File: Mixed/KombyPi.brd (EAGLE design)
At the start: 63.2 x 57.1 mm, 16 parts, among them IC3 DS1307, J1 POWER_JACKPTH, J2 MOLEX-39501XXX4, Q1 32.768

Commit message: Update KombyPi mixed boards to be cleaner layout.
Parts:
- removed BAT: CR1220, adafruit:CR1220-THM
- removed C1: 0.1uF, adafruit:C025-025X050
- removed IC3: DS1307, adafruit:DIL08
- removed JP3: RASPBERRYPI-B+-GPIO, SparkFun-Boards:2X20-SHROUDED
- removed Q1: 32.768, crystal:TC38H
- added JP1: RASPBERRYPI-GPIOPTH, SparkFun-Boards:2X13-SHROUDED
- added U$2: (no value), holes:3,6
- added U$3: (no value), DIYChristmas-org:DIYC
- U$1: device DIYChristmas-org:DIYC -> holes:3,6
- moved C4 55.4 mm to (7.62, 38.1), turned to 270 degrees
- moved C2 52.4 mm to (54.6, 50.8)
- moved C3 40.9 mm to (47.0, 50.8)
- moved J2 39.6 mm to (30.5, 6.35), turned to 0 degrees
- moved V1 33.8 mm to (20.3, 38.1), turned to 0 degrees
- moved F2 24.4 mm to (30.5, 16.5), turned to 180 degrees
- moved JP4 19.1 mm to (50.8, 40.6)
- moved U$1 13.5 mm to (29.2, 25.4)
- moved FTDI 6.35 mm to (8.89, 17.8), turned to 0 degrees
- moved D1 1.80 mm to (17.8, 5.08)
- moved J1 1.27 mm to (7.62, -3.17)
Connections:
- removed net N$14: IC3.1, Q1.2
- removed net N$15: IC3.2, Q1.1
- removed net N$39: BAT.+2, IC3.3
- removed net SQW: IC3.7
- new net WS2801_VCC_FUSED: F2.P$1, F2.P$2, J2.4
- net 3.3V: now also JP1.1, JP1.17; no longer JP3.1, JP3.17
- net CE0: now also JP1.24; no longer JP3.24
- net CE1: now also JP1.26; no longer JP3.26
- net GND: now also JP1.14, JP1.20, JP1.25, JP1.6, JP1.9; no longer BAT.-, C1.2, IC3.4, JP3.14, JP3.20, JP3.25, JP3.30, JP3.34, JP3.39, JP3.6, JP3.9
- net MISO: now also JP1.21; no longer JP3.21
- net MOSI: now also JP1.19; no longer JP3.19
- net RF_CE: now also JP1.15; no longer JP3.15
- net RXI: now also JP1.10; no longer JP3.10
- net SCL: now also JP1.5; no longer IC3.6, JP3.5
- net SCLK: now also JP1.23; no longer JP3.23
- net SDA: now also JP1.3; no longer IC3.5, JP3.3
- net TXO: now also JP1.8; no longer JP3.8
- net VCC: now also JP1.2, JP1.4; no longer C1.1, D1.C, F2.P$3, F2.P$4, IC3.8, JP3.2, JP3.4
- net WS2801_VCC: now also D1.C, F2.P$3, F2.P$4; no longer F2.P$1, F2.P$2, J2.4
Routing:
- net N$39: track 33.0 -> 0.00 mm
- net CE1: track 58.4 -> 27.0 mm, vias 1 -> 0
- net MOSI: track 34.0 -> 59.1 mm
- net MISO: track 9.94 -> 34.6 mm
- net SDA: track 24.2 -> 0.00 mm
- net SCL: track 23.5 -> 0.00 mm
- net WS2801_SCLK: track 16.1 -> 35.1 mm
- net N$3: track 0.00 -> 17.7 mm
- net WS2801_MOSI: track 20.2 -> 37.5 mm
- net RF_CE: track 15.0 -> 31.9 mm, vias 0 -> 1
- net WS2801_VCC_FUSED: track 0.00 -> 13.8 mm
- net 3.3V: track 29.2 -> 42.1 mm, vias 0 -> 1
- net SCLK: track 50.5 -> 61.6 mm
- net TXO: track 43.8 -> 53.1 mm
- net N$14: track 8.45 -> 0.00 mm
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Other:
- board size 63.2 x 57.1 mm -> 59.4 x 57.1 mm
- board text added: "(c) 2015 Mat Mrosko"
- board text added: "B"
- board text added: "B+"

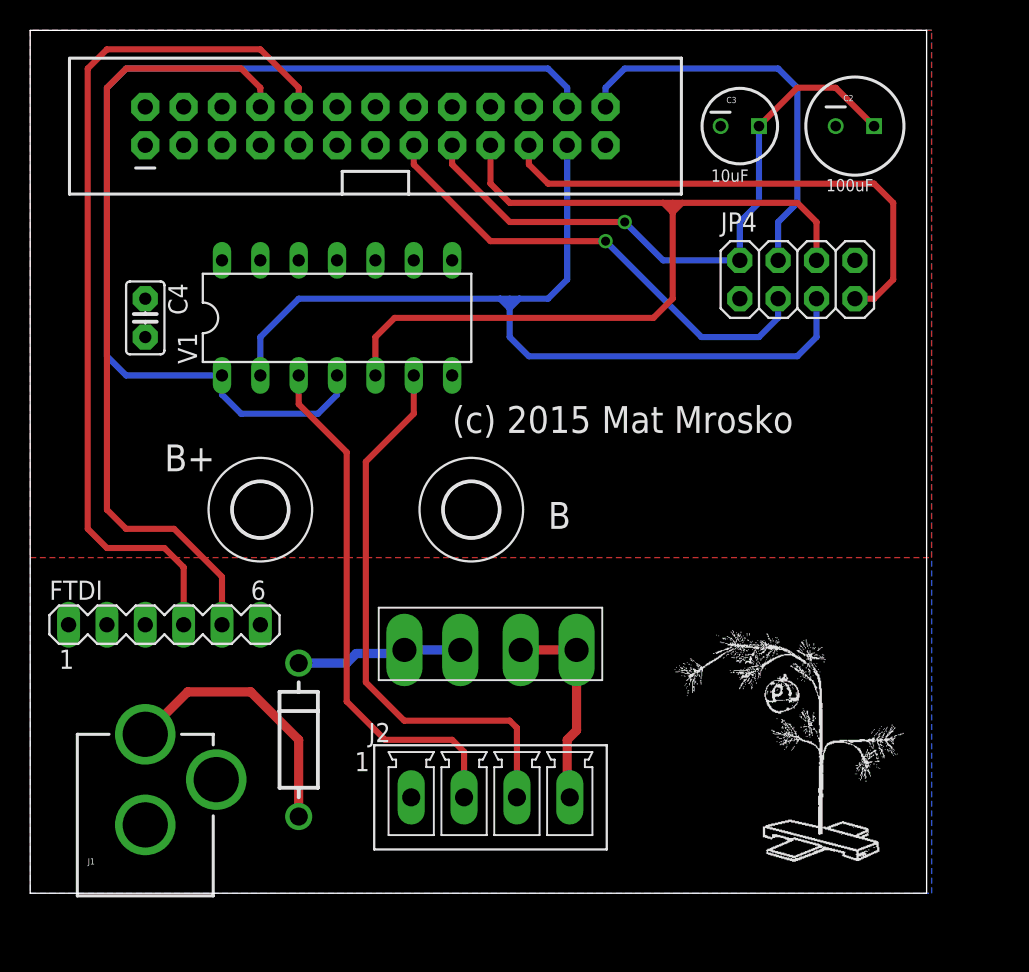
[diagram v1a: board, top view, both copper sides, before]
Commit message: Update KombyPi to have proper orientation for nRF
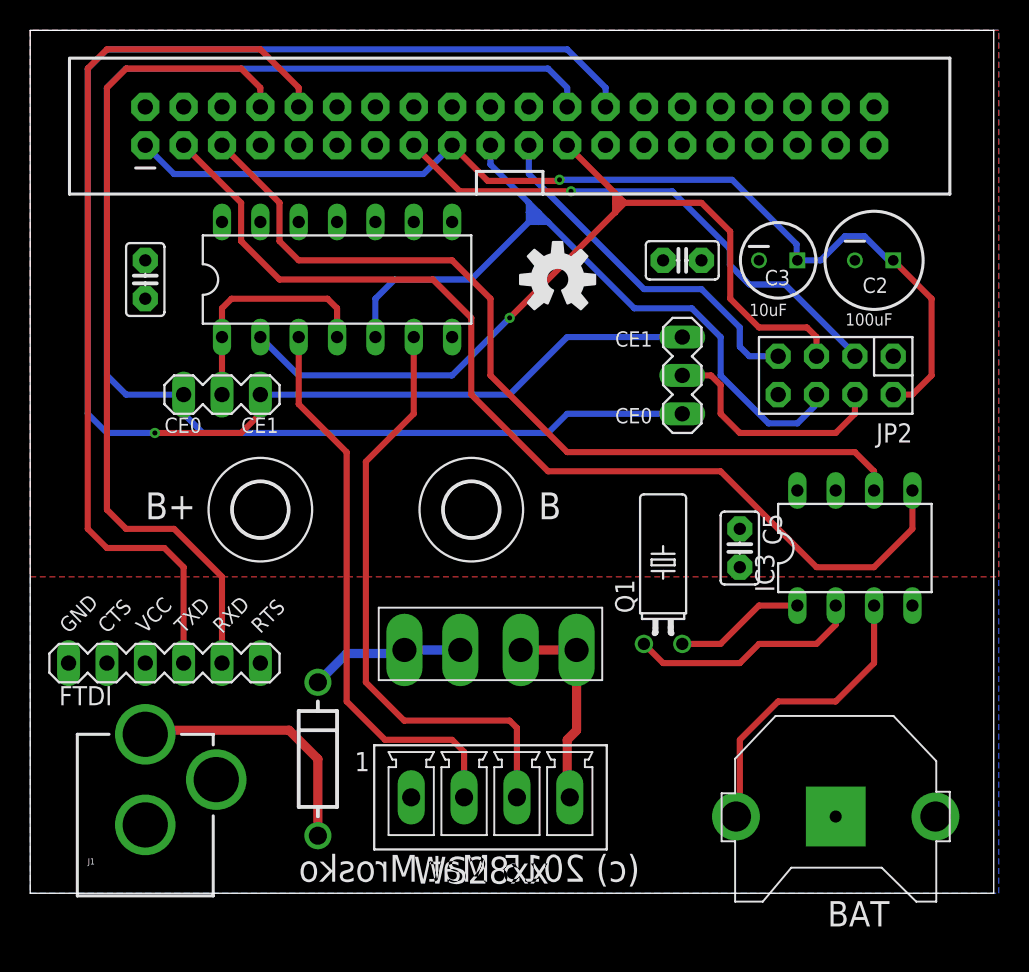
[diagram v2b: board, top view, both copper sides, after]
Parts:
- removed JP4: (no value), adafruit:2X04
- added BAT: CR1220, adafruit:CR1220-THM
- added C1, C5: 0.1uF, adafruit:C025-025X050
- added IC3: DS1307, adafruit:DIL08
- added JP2: (no value), Materdaddy-Custom:2X04
- added Q1: 32.768, crystal:TC38H
- added SV1, SV2: (no value), Materdaddy-Custom:MA03-1
- FTDI: device con-lstb:MA06-1 -> Materdaddy-Custom:MA06-1
- JP1: value RASPBERRYPI-GPIOPTH -> RASPBERRYPI-B+-GPIO; device SparkFun-Boards:2X13-SHROUDED -> SparkFun-Boards:2X20-SHROUDED
- U$3: device DIYChristmas-org:DIYC -> SparkFun-Aesthetics:OSHW-LOGO-M
- moved U$3 40.0 mm to (34.9, 40.6)
- moved C3 9.25 mm to (49.5, 41.9)
- moved C2 8.98 mm to (55.9, 41.9)
- moved JP1 8.89 mm to (31.8, 50.8)
- moved FTDI 2.54 mm to (8.89, 15.2)
- moved C4 2.54 mm to (7.62, 40.6)
- moved V1 2.54 mm to (20.3, 40.6)
- moved D1 1.80 mm to (19.1, 3.81)
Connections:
- new net +3V3: C1.1
- new net N$14: IC3.1, Q1.2
- new net N$15: IC3.2, Q1.1
- new net N$39: BAT.+2, IC3.3
- new net NRF_CE: JP2.4, SV1.2
- new net SQW: IC3.7
- new net WS_CE: SV2.2, V1.1, V1.4
- net 3.3V: now also JP2.2; no longer JP4.2
- net CE0: now also SV1.1, SV2.1; no longer V1.1, V1.4
- net CE1: now also SV1.3, SV2.3; no longer JP4.4
- net GND: now also BAT.-, C1.2, C5.2, IC3.4, JP1.30, JP1.34, JP1.39, JP2.1; no longer JP4.1
- net MISO: now also JP2.7; no longer JP4.7
- net MOSI: now also JP2.6; no longer JP4.6
- net RF_CE: now also JP2.3; no longer JP4.3
- net SCL: now also IC3.6
- net SCLK: now also JP2.5; no longer JP4.5
- net SDA: now also IC3.5
- net VCC: now also C5.1, IC3.8
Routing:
- net CE1: track 27.0 -> 103.3 mm, vias 0 -> 1
- net SDA: track 0.00 -> 67.9 mm
- net SCL: track 0.00 -> 57.9 mm
- net 3.3V: track 42.1 -> 68.0 mm
- net CE0: track 69.9 -> 92.8 mm
- net N$39: track 0.00 -> 20.0 mm
- net NRF_CE: track 0.00 -> 15.9 mm
- net WS_CE: track 0.00 -> 15.8 mm
- net N$15: track 0.00 -> 15.5 mm
- net MISO: track 34.6 -> 24.2 mm
- net N$14: track 0.00 -> 8.67 mm
- net MOSI: track 59.1 -> 52.1 mm
- net SCLK: track 61.6 -> 57.5 mm, vias 0 -> 1
- net RF_CE: track 31.9 -> 35.7 mm
- net WS2801_SCLK: track 35.1 -> 37.6 mm
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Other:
- board size 59.4 x 57.1 mm -> 63.8 x 57.1 mm
- board text added: "CE0"
- board text added: "CE1"
- board text added: "CTS"
- board text added: "GND"
- board text added: "RTS"
- board text added: "RXD"
- board text added: "TXD"
- board text added: "VCC"
- board text added: "WS28xx"
